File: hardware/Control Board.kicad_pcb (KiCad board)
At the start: 2 copper layers, 68.4 x 53.1 mm, 42 parts, among them J1 Conn_FTDI, J2 SOLAR, M1 MOTOR, Q1 IRF7105PbF, Q2 BC817W, Q3 BC817W, Q4 IRF7105PbF, SW1 SW_Push, SW2 SW_Push, SW3 SW_Push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

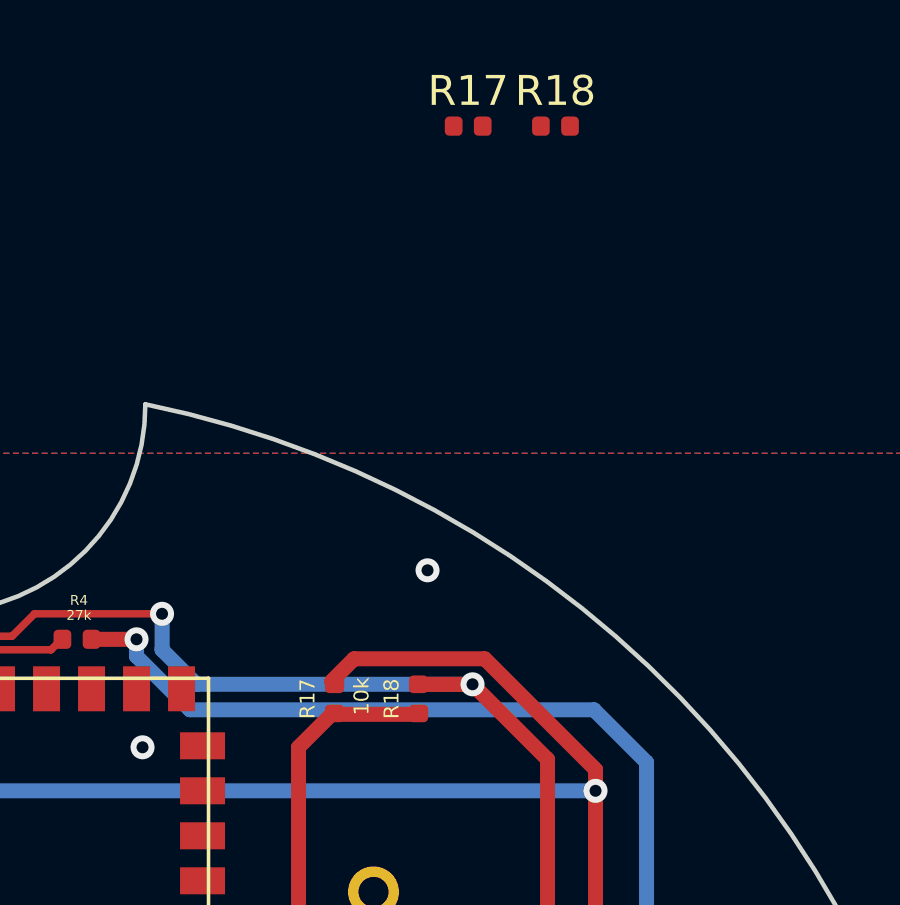
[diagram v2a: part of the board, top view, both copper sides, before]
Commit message: Fixing silkscreen on pull ups
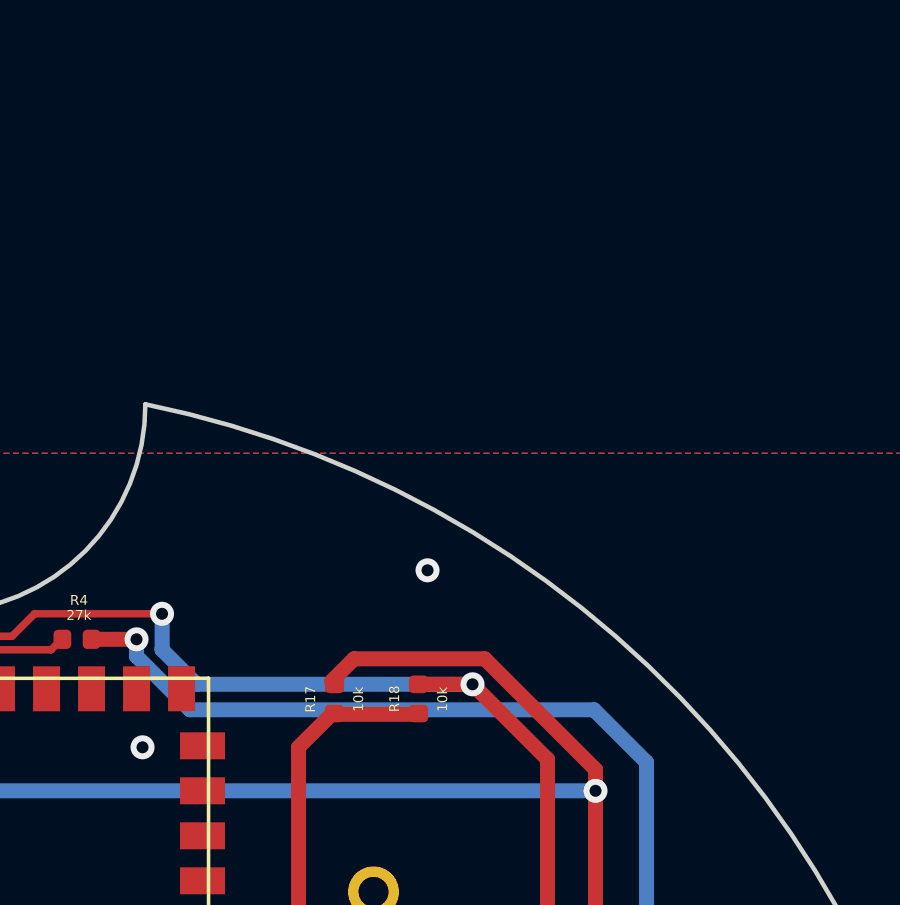
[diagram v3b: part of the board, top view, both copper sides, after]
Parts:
- removed the R17 at (126.7, 87.6)
- removed the R18 at (129.6, 87.6)
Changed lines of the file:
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@@
     (add_net WATER_ON)
-  )
-  (module Resistor_SMD:R_0402_1005Metric (layer F.Cu)
-    (at 129.565001 87.595001)
-    (descr "Resistor SMD 0402 (1005 Metric), square (rectangular) end terminal, IPC_7351 nominal, (Body size source: http://www.tortai-tech.com/upload/download/2011102023233369053.pdf), generated with kicad-footprint-generator")
-    (tags resistor)
-    (attr smd)
-    (fp_text reference R18 (at 0 -1.17) (layer F.SilkS)
-      (effects (font (size 1 1) (thickness 0.15)))
-    )
-    (fp_text value 10k (at 0 1.17) (layer F.Fab)
-      (effects (font (size 1 1) (thickness 0.15)))
-    )
-    (fp_text user %R (at 0 0) (layer F.Fab)
-      (effects (font (size 0.25 0.25) (thickness 0.04)))
-    )
-    (fp_line (start -0.5 0.25) (end -0.5 -0.25) (layer F.Fab) (width 0.1))
-    (fp_line (start -0.5 -0.25) (end 0.5 -0.25) (layer F.Fab) (width 0.1))
-    (fp_line (start 0.5 -0.25) (end 0.5 0.25) (layer F.Fab) (width 0.1))
-    (fp_line (start 0.5 0.25) (end -0.5 0.25) (layer F.Fab) (width 0.1))
-    (fp_line (start -0.93 0.47) (end -0.93 -0.47) (layer F.CrtYd) (width 0.05))
-    (fp_line (start -0.93 -0.47) (end 0.93 -0.47) (layer F.CrtYd) (width 0.05))
-    (fp_line (start 0.93 -0.47) (end 0.93 0.47) (layer F.CrtYd) (width 0.05))
-    (fp_line (start 0.93 0.47) (end -0.93 0.47) (layer F.CrtYd) (width 0.05))
-    (pad 2 smd roundrect (at 0.485 0) (size 0.59 0.64) (layers F.Cu F.Paste F.Mask) (roundrect_rratio 0.25)
-      (net 9 EN))
-    (pad 1 smd roundrect (at -0.485 0) (size 0.59 0.64) (layers F.Cu F.Paste F.Mask) (roundrect_rratio 0.25)
-      (net 3 +3V3))
-    (model ${KISYS3DMOD}/Resistor_SMD.3dshapes/R_0402_1005Metric.wrl
-      (at (xyz 0 0 0))
-      (scale (xyz 1 1 1))
-      (rotate (xyz 0 0 0))
-    )
-  )
-  (module Resistor_SMD:R_0402_1005Metric (layer F.Cu)
-    (at 126.655001 87.595001)
-    (descr "Resistor SMD 0402 (1005 Metric), square (rectangular) end terminal, IPC_7351 nominal, (Body size source: http://www.tortai-tech.com/upload/download/2011102023233369053.pdf), generated with kicad-footprint-generator")
-    (tags resistor)
-    (attr smd)
-    (fp_text reference R17 (at 0 -1.17) (layer F.SilkS)
-      (effects (font (size 1 1) (thickness 0.15)))
-    )
-    (fp_text value 10k (at 0 1.17) (layer F.Fab)
-      (effects (font (size 1 1) (thickness 0.15)))
-    )
-    (fp_text user %R (at 0 0) (layer F.Fab)
-      (effects (font (size 0.25 0.25) (thickness 0.04)))
-    )
-    (fp_line (start -0.5 0.25) (end -0.5 -0.25) (layer F.Fab) (width 0.1))
-    (fp_line (start -0.5 -0.25) (end 0.5 -0.25) (layer F.Fab) (width 0.1))
-    (fp_line (start 0.5 -0.25) (end 0.5 0.25) (layer F.Fab) (width 0.1))
-    (fp_line (start 0.5 0.25) (end -0.5 0.25) (layer F.Fab) (width 0.1))
-    (fp_line (start -0.93 0.47) (end -0.93 -0.47) (layer F.CrtYd) (width 0.05))
-    (fp_line (start -0.93 -0.47) (end 0.93 -0.47) (layer F.CrtYd) (width 0.05))
-    (fp_line (start 0.93 -0.47) (end 0.93 0.47) (layer F.CrtYd) (width 0.05))
-    (fp_line (start 0.93 0.47) (end -0.93 0.47) (layer F.CrtYd) (width 0.05))
-    (pad 2 smd roundrect (at 0.485 0) (size 0.59 0.64) (layers F.Cu F.Paste F.Mask) (roundrect_rratio 0.25)
-      (net 10 IO0))
-    (pad 1 smd roundrect (at -0.485 0) (size 0.59 0.64) (layers F.Cu F.Paste F.Mask) (roundrect_rratio 0.25)
-      (net 3 +3V3))
-    (model ${KISYS3DMOD}/Resistor_SMD.3dshapes/R_0402_1005Metric.wrl
-      (at (xyz 0 0 0))
-      (scale (xyz 1 1 1))
-      (rotate (xyz 0 0 0))
-    )
   )
   (module Package_DFN_QFN:Texas_S-PVQFN-N16_EP2.7x2.7mm (layer F.Cu)
@@
     (tags resistor)
     (attr smd)
-    (fp_text reference R17 (at 0 -0.9 90) (layer F.SilkS)
-      (effects (font (size 0.5 0.5) (thickness 0.125)))
-    )
-    (fp_text value 10k (at 0.085 0.9 90) (layer F.SilkS)
-      (effects (font (size 0.5 0.5) (thickness 0.125)))
+    (fp_text reference R17 (at -0.015 -0.8 90) (layer F.SilkS)
+      (effects (font (size 0.33 0.33) (thickness 0.0825)))
+    )
+    (fp_text value 10k (at -0.015 0.8 90) (layer F.SilkS)
+      (effects (font (size 0.33 0.33) (thickness 0.0825)))
     )
     (fp_line (start 0.93 0.47) (end -0.93 0.47) (layer F.CrtYd) (width 0.05))
@@
     (tags resistor)
     (attr smd)
-    (fp_text reference R18 (at 0 -0.9 90) (layer F.SilkS)
-      (effects (font (size 0.5 0.5) (thickness 0.125)))
-    )
-    (fp_text value 10k (at 0.085 0.9 90) (layer B.Paste)
-      (effects (font (size 0.5 0.5) (thickness 0.125)))
-    )
-    (fp_text user %R (at 0 0 90) (layer F.Fab)
+    (fp_text reference R18 (at 0 -0.8 90) (layer F.SilkS)
+      (effects (font (size 0.33 0.33) (thickness 0.0825)))
+    )
+    (fp_text value 10k (at -0.015 0.8 90) (layer F.SilkS)
+      (effects (font (size 0.33 0.33) (thickness 0.0825)))
+    )
+    (fp_text user %R (at 0 0 90) (layer F.Fab)

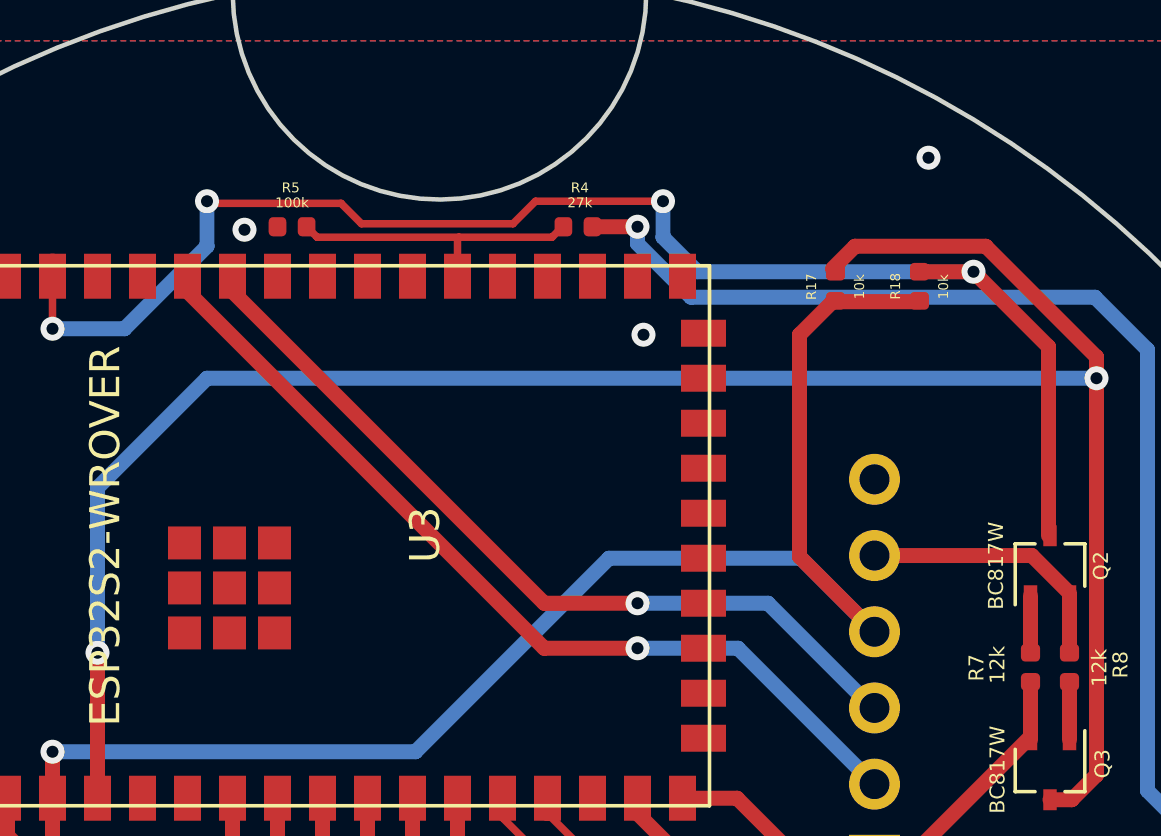
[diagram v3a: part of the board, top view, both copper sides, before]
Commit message: RX and TX were crossing over, adding spots for capacitors on EN and IO0
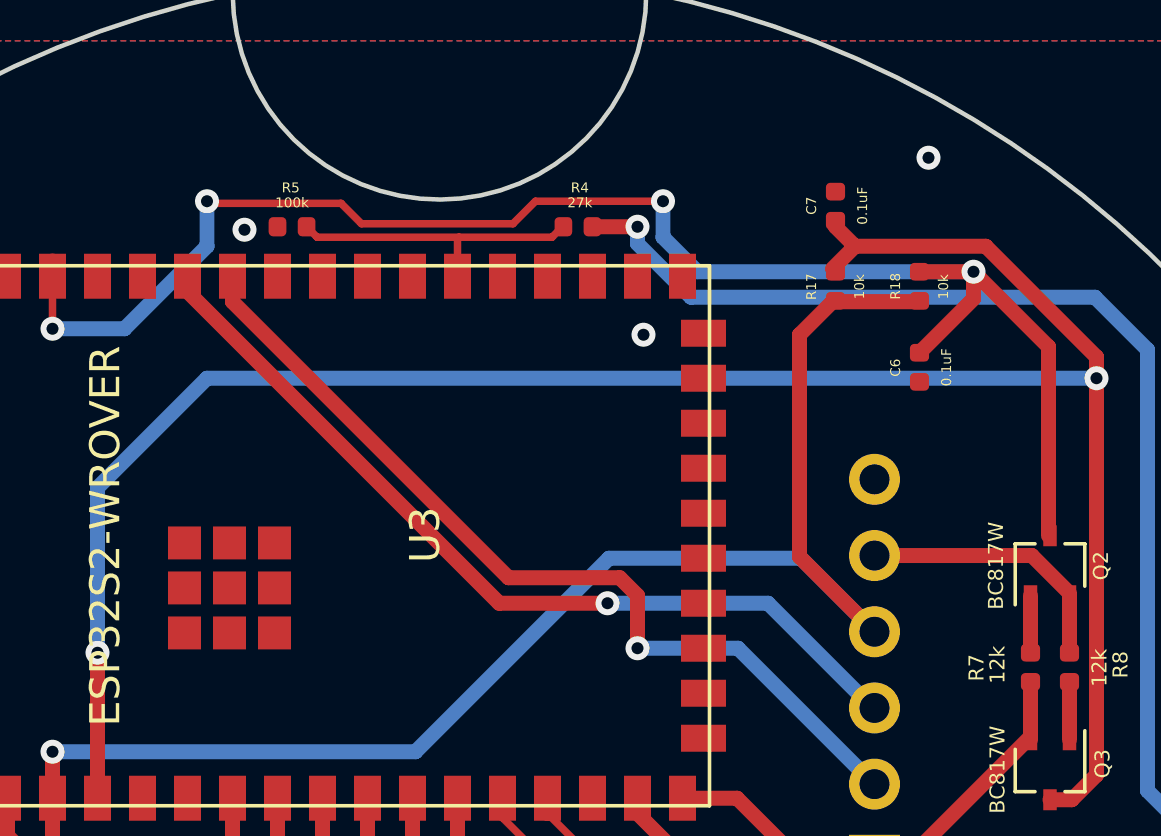
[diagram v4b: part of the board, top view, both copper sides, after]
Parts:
- added C6: 0.1uF, Capacitor_SMD:C_0402_1005Metric, F.Cu at (125.0, 109.4)
- added C7: 0.1uF, Capacitor_SMD:C_0402_1005Metric, F.Cu at (122.2, 104.0)
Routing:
- net EN: track 49.5 -> 53.0 mm
- net TX: track 27.7 -> 29.6 mm
- net IO0: track 71.6 -> 72.7 mm
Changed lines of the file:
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@@
     (thickness 1.6)
     (drawings 57)
-    (tracks 268)
+    (tracks 275)
     (zones 0)
-    (modules 40)
+    (modules 42)
     (nets 54)
   )
@@
       (net 3 +3V3))
     (model ${KISYS3DMOD}/Resistor_SMD.3dshapes/R_0402_1005Metric.wrl
+      (at (xyz 0 0 0))
+      (scale (xyz 1 1 1))
+      (rotate (xyz 0 0 0))
+    )
+  )
+  (module Capacitor_SMD:C_0402_1005Metric (layer F.Cu)
+    (at 125 109.385 270)
+    (descr "Capacitor SMD 0402 (1005 Metric), square (rectangular) end terminal, IPC_7351 nominal, (Body size source: http://www.tortai-tech.com/upload/download/2011102023233369053.pdf), generated with kicad-footprint-generator")
+    (tags capacitor)
+    (attr smd)
+    (fp_text reference C6 (at 0.015 0.8 90) (layer F.SilkS)
+      (effects (font (size 0.33 0.33) (thickness 0.0825)))
+    )
+    (fp_text value 0.1uF (at 0 -0.9 90) (layer F.SilkS)
+      (effects (font (size 0.33 0.33) (thickness 0.0825)))
+    )
+    (fp_line (start 0.93 0.47) (end -0.93 0.47) (layer F.CrtYd) (width 0.05))
+    (fp_line (start 0.93 -0.47) (end 0.93 0.47) (layer F.CrtYd) (width 0.05))
+    (fp_line (start -0.93 -0.47) (end 0.93 -0.47) (layer F.CrtYd) (width 0.05))
+    (fp_line (start -0.93 0.47) (end -0.93 -0.47) (layer F.CrtYd) (width 0.05))
+    (fp_line (start 0.5 0.25) (end -0.5 0.25) (layer F.Fab) (width 0.1))
+    (fp_line (start 0.5 -0.25) (end 0.5 0.25) (layer F.Fab) (width 0.1))
+    (fp_line (start -0.5 -0.25) (end 0.5 -0.25) (layer F.Fab) (width 0.1))
+    (fp_line (start -0.5 0.25) (end -0.5 -0.25) (layer F.Fab) (width 0.1))
+    (fp_text user %R (at 0 0 90) (layer F.Fab)
+      (effects (font (size 0.25 0.25) (thickness 0.04)))
+    )
+    (pad 1 smd roundrect (at -0.485 0 270) (size 0.59 0.64) (layers F.Cu F.Paste F.Mask) (roundrect_rratio 0.25)
+      (net 9 EN))
+    (pad 2 smd roundrect (at 0.485 0 270) (size 0.59 0.64) (layers F.Cu F.Paste F.Mask) (roundrect_rratio 0.25)
+      (net 1 GND))
+    (model ${KISYS3DMOD}/Capacitor_SMD.3dshapes/C_0402_1005Metric.wrl
+      (at (xyz 0 0 0))
+      (scale (xyz 1 1 1))
+      (rotate (xyz 0 0 0))
+    )
+  )
+  (module Capacitor_SMD:C_0402_1005Metric (layer F.Cu)
+    (at 122.2 104.015 90)
+    (descr "Capacitor SMD 0402 (1005 Metric), square (rectangular) end terminal, IPC_7351 nominal, (Body size source: http://www.tortai-tech.com/upload/download/2011102023233369053.pdf), generated with kicad-footprint-generator")
+    (tags capacitor)
+    (attr smd)
+    (fp_text reference C7 (at 0.015 -0.8 90) (layer F.SilkS)
+      (effects (font (size 0.33 0.33) (thickness 0.0825)))
+    )
+    (fp_text value 0.1uF (at 0.015 0.9 90) (layer F.SilkS)
+      (effects (font (size 0.33 0.33) (thickness 0.0825)))
+    )
+    (fp_text user %R (at 0 0 90) (layer F.Fab)
+      (effects (font (size 0.25 0.25) (thickness 0.04)))
+    )
+    (fp_line (start -0.5 0.25) (end -0.5 -0.25) (layer F.Fab) (width 0.1))
+    (fp_line (start -0.5 -0.25) (end 0.5 -0.25) (layer F.Fab) (width 0.1))
+    (fp_line (start 0.5 -0.25) (end 0.5 0.25) (layer F.Fab) (width 0.1))
+    (fp_line (start 0.5 0.25) (end -0.5 0.25) (layer F.Fab) (width 0.1))
+    (fp_line (start -0.93 0.47) (end -0.93 -0.47) (layer F.CrtYd) (width 0.05))
+    (fp_line (start -0.93 -0.47) (end 0.93 -0.47) (layer F.CrtYd) (width 0.05))
+    (fp_line (start 0.93 -0.47) (end 0.93 0.47) (layer F.CrtYd) (width 0.05))
+    (fp_line (start 0.93 0.47) (end -0.93 0.47) (layer F.CrtYd) (width 0.05))
+    (pad 2 smd roundrect (at 0.485 0 90) (size 0.59 0.64) (layers F.Cu F.Paste F.Mask) (roundrect_rratio 0.25)
+      (net 1 GND))
+    (pad 1 smd roundrect (at -0.485 0 90) (size 0.59 0.64) (layers F.Cu F.Paste F.Mask) (roundrect_rratio 0.25)
+      (net 10 IO0))
+    (model ${KISYS3DMOD}/Capacitor_SMD.3dshapes/C_0402_1005Metric.wrl
       (at (xyz 0 0 0))
       (scale (xyz 1 1 1))
@@
   (segment (start 106.4 104.6) (end 111.449999 104.6) (width 0.25) (layer F.Cu) (net 9))
   (segment (start 125 106.2) (end 126.8 106.2) (width 0.5) (layer F.Cu) (net 9))
+  (segment (start 126.8 107.1) (end 126.8 106.2) (width 0.5) (layer F.Cu) (net 9))
+  (segment (start 125 108.9) (end 126.8 107.1) (width 0.5) (layer F.Cu) (net 9))
   (via (at 130.9 109.75) (size 0.8) (drill 0.4) (layers F.Cu B.Cu) (net 10))
   (via (at 97.6 118.9) (size 0.8) (drill 0.4) (layers F.Cu B.Cu) (net 10))
@@
   (segment (start 130.9 109.75) (end 130.9 109.041998) (width 0.5) (layer F.Cu) (net 10))
   (segment (start 122.850001 105.349999) (end 122.1 106.1) (width 0.5) (layer F.Cu) (net 10))
+  (segment (start 122.2 104.699998) (end 122.850001 105.349999) (width 0.5) (layer F.Cu) (net 10))
+  (segment (start 122.2 104.5) (end 122.2 104.699998) (width 0.5) (layer F.Cu) (net 10))
   (segment (start 128.7 119.87) (end 128.7 121.8) (width 0.5) (layer F.Cu) (net 11))
   (segment (start 123.5 125.82) (end 124.58 125.82) (width 0.5) (layer F.Cu) (net 11))
@@
   (segment (start 113.0125 126.3125) (end 111.1 124.4) (width 0.25) (layer F.Cu) (net 14))
   (segment (start 111.1 124.4) (end 111.1 123.8) (width 0.25) (layer F.Cu) (net 14))
-  (via (at 115.6 117.25) (size 0.8) (drill 0.4) (layers F.Cu B.Cu) (net 29))
-  (segment (start 115.6 117.25) (end 119.95 117.25) (width 0.5) (layer B.Cu) (net 29))
-  (segment (start 119.95 117.25) (end 123.5 120.8) (width 0.5) (layer B.Cu) (net 29))
-  (segment (start 112.489998 117.25) (end 102.1 106.860002) (width 0.5) (layer F.Cu) (net 29))
-  (segment (start 115.6 117.25) (end 112.489998 117.25) (width 0.5) (layer F.Cu) (net 29))
-  (segment (start 102.1 106.860002) (end 102.1 106.3) (width 0.5) (layer F.Cu) (net 29))
   (via (at 115.6 118.75) (size 0.8) (drill 0.4) (layers F.Cu B.Cu) (net 30))
   (segment (start 115.6 118.75) (end 118.95 118.75) (width 0.5) (layer B.Cu) (net 30))
   (segment (start 118.95 118.75) (end 123.5 123.3) (width 0.5) (layer B.Cu) (net 30))
-  (segment (start 112.489998 118.75) (end 100.6 106.860002) (width 0.5) (layer F.Cu) (net 30))
-  (segment (start 115.6 118.75) (end 112.489998 118.75) (width 0.5) (layer F.Cu) (net 30))
-  (segment (start 100.6 106.860002) (end 100.6 106.3) (width 0.5) (layer F.Cu) (net 30))
+  (segment (start 100.6 106.860002) (end 100.6 106.3) (width 0.5) (layer F.Cu) (net 29))
+  (segment (start 119.95 117.25) (end 123.5 120.8) (width 0.5) (layer B.Cu) (net 29))
+  (segment (start 114.6 117.25) (end 119.95 117.25) (width 0.5) (layer B.Cu) (net 29))
+  (via (at 114.6 117.25) (size 0.8) (drill 0.4) (layers F.Cu B.Cu) (net 29))
+  (segment (start 110.989998 117.25) (end 100.6 106.860002) (width 0.5) (layer F.Cu) (net 29))
+  (segment (start 114.6 117.25) (end 110.989998 117.25) (width 0.5) (layer F.Cu) (net 29))
+  (segment (start 100.6 106.860002) (end 100.6 106.5) (width 0.5) (layer F.Cu) (net 29))
+  (segment (start 115.6 118.75) (end 115.6 116.991998) (width 0.5) (layer F.Cu) (net 30))
+  (segment (start 115.008001 116.399999) (end 115.6 116.991998) (width 0.5) (layer F.Cu) (net 30))
+  (segment (start 111.299999 116.399999) (end 115.008001 116.399999) (width 0.5) (layer F.Cu) (net 30))
+  (segment (start 102.1 107.2) (end 111.299999 116.399999) (width 0.5) (layer F.Cu) (net 30))
+  (segment (start 102.1 106.35) (end 102.1 107.2) (width 0.5) (layer F.Cu) (net 30))
   (segment (start 128.65 128.483332) (end 129.883332 128.483332) (width 0.5) (layer F.Cu) (net 32))
   (segment (start 128.65 128.483332) (end 121.083332 128.483332) (width 0.5) (layer F.Cu) (net 32))
